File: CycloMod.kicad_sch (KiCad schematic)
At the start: 72 parts, among them J1 MICROMOD-2222, U1 10CL010YM164, U2 W25Q128JVS, U3 1.2V, U4 RP2350_60QFN, U5 MIC5504-2.5YMT, Y1 ABM8-272-T3

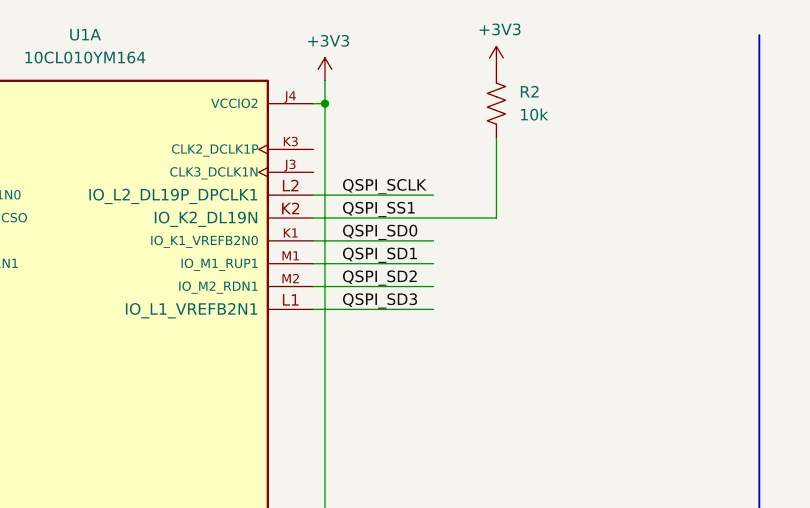
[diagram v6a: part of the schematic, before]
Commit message: remaped QSPI pins, checking in before moving flash
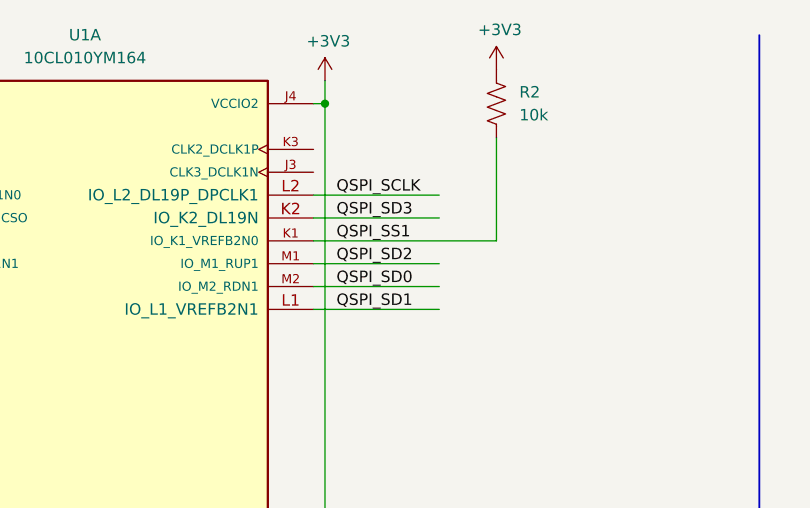
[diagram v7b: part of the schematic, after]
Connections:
- net QSPI_SD0: now also U1.M2 (IO_M2_RDN1); no longer U1.K1 (IO_K1_VREFB2N0)
- net QSPI_SD1: now also U1.L1 (IO_L1_VREFB2N1); no longer U1.M1 (IO_M1_RUP1)
- net QSPI_SD2: now also U1.M1 (IO_M1_RUP1); no longer U1.M2 (IO_M2_RDN1)
- net QSPI_SD3: now also U1.K2 (IO_K2_DL19N); no longer U1.L1 (IO_L1_VREFB2N1)
- net QSPI_SS1: now also U1.K1 (IO_K1_VREFB2N0); no longer U1.K2 (IO_K2_DL19N)
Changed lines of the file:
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@@
 	(wire
 		(pts
-			(xy 316.865 48.26) (xy 303.53 48.26)
+			(xy 317.5 48.26) (xy 303.53 48.26)
 		)
 		(stroke
@@
 	(wire
 		(pts
+			(xy 303.53 40.64) (xy 323.85 40.64)
+		)
+		(stroke
+			(width 0)
+			(type default)
+		)
+	)
+	(wire
+		(pts
 			(xy 147.32 59.69) (xy 158.75 59.69)
 		)
@@
 	(wire
 		(pts
+			(xy 303.53 38.1) (xy 317.5 38.1)
+		)
+		(stroke
+			(width 0)
+			(type default)
+		)
+	)
+	(wire
+		(pts
 			(xy 95.25 186.69) (xy 90.17 186.69)
 		)
@@
 	(wire
 		(pts
-			(xy 303.53 38.1) (xy 323.85 38.1)
-		)
-		(stroke
-			(width 0)
-			(type default)
-		)
-	)
-	(wire
-		(pts
 			(xy 397.51 116.84) (xy 397.51 121.92)
 		)
@@
 	(wire
 		(pts
-			(xy 303.53 35.56) (xy 316.865 35.56)
+			(xy 303.53 35.56) (xy 317.5 35.56)
 		)
 		(stroke
@@
 	(wire
 		(pts
-			(xy 303.53 40.64) (xy 316.865 40.64)
-		)
-		(stroke
-			(width 0)
-			(type default)
-		)
-	)
-	(wire
-		(pts
 			(xy 302.895 245.11) (xy 304.8 245.11)
 		)
@@
 	(wire
 		(pts
-			(xy 323.85 29.21) (xy 323.85 38.1)
+			(xy 323.85 29.21) (xy 323.85 40.64)
 		)
 		(stroke
@@
 	(wire
 		(pts
-			(xy 303.53 43.18) (xy 316.865 43.18)
+			(xy 303.53 43.18) (xy 317.5 43.18)
 		)
 		(stroke
@@
 	(wire
 		(pts
-			(xy 303.53 45.72) (xy 316.865 45.72)
+			(xy 303.53 45.72) (xy 317.5 45.72)
 		)
 		(stroke
@@
 	)
 	(label "QSPI_SCLK"
-		(at 306.705 35.56 0)
+		(at 306.07 35.56 0)
 		(fields_autoplaced yes)
 		(effects
@@
 	)
 	(label "QSPI_SD2"
-		(at 306.705 45.72 0)
+		(at 306.07 43.18 0)
 		(fields_autoplaced yes)
 		(effects
@@
 	)
 	(label "QSPI_SD3"
-		(at 306.705 48.26 0)
+		(at 306.07 38.1 0)
 		(fields_autoplaced yes)
 		(effects
@@
 	)
 	(label "QSPI_SD1"
-		(at 306.705 43.18 0)
+		(at 306.07 48.26 0)
 		(fields_autoplaced yes)
 		(effects
@@
 	)
 	(label "QSPI_SS1"
-		(at 306.705 38.1 0)
+		(at 306.07 40.64 0)
 		(fields_autoplaced yes)
 		(effects
@@
 	)
 	(label "QSPI_SD0"
-		(at 306.705 40.64 0)
+		(at 306.07 45.72 0)
 		(fields_autoplaced yes)
 		(effects

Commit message: all connected, cleaning up
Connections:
- net GND: now also J1.GND; no longer J1.GND1 (GND), J1.GND2 (GND), J1.GND3 (GND)
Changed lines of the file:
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@@
 		(pin "9"
 		)
-		(pin "GND1"
-		)
-		(pin "GND2"
-		)
-		(pin "GND3"
+		(pin "GND"
 		)
 		(instances
